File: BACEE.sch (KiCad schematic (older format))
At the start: 13 parts, among them U1 DS1337S+, U2 24LC1025, U3 24LC1025, U4 ATMEGA328P-AU, Y1 Crystal 32MHz, Y2 Crystal 16MHz

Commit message: Corrected the Atmega unconnected pins
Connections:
- no-connect marks 13 -> 7
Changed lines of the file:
@@
 	7800 4950 7800 5150
 $Comp
-L power:GNDPWR #PWR?
+L power:GNDPWR #PWR0101
 U 1 1 5EC52C1A
 P 4950 7400
-F 0 "#PWR?" H 4950 7200 50  0001 C CNN
+F 0 "#PWR0101" H 4950 7200 50  0001 C CNN
 F 1 "GNDPWR" H 4954 7246 50  0000 C CNN
 F 2 "" H 4950 7350 50  0001 C CNN
@@
 	650  1600 650  1650
 $Comp
-L power:GNDPWR #PWR?
+L power:GNDPWR #PWR0102
 U 1 1 5EC62315
 P 2100 2750
-F 0 "#PWR?" H 2100 2550 50  0001 C CNN
+F 0 "#PWR0102" H 2100 2550 50  0001 C CNN
 F 1 "GNDPWR" H 2104 2596 50  0000 C CNN
 F 2 "" H 2100 2700 50  0001 C CNN
@@
 Wire Wire Line
 	2750 2100 2900 2100
-NoConn ~ 2800 1700
 Text Label 2800 3900 2    50   ~ 0
 Vcc
@@
 	2750 3900 2800 3900
 $Comp
-L power:GNDPWR #PWR?
+L power:GNDPWR #PWR0103
 U 1 1 5EC69D54
 P 2750 5300
-F 0 "#PWR?" H 2750 5100 50  0001 C CNN
+F 0 "#PWR0103" H 2750 5100 50  0001 C CNN
 F 1 "GNDPWR" H 2754 5146 50  0000 C CNN
 F 2 "" H 2750 5250 50  0001 C CNN
@@
 Wire Wire Line
 	2750 4200 3350 4200
-Wire Wire Line
-	2000 4200 2750 4200
 Text Label 2400 4500 0    50   ~ 0
 SDA
@@
 ADDS2
 $Comp
-L power:GNDPWR #PWR?
+L power:GNDPWR #PWR0104
 U 1 1 5EC78DFA
 P 9750 3500
-F 0 "#PWR?" H 9750 3300 50  0001 C CNN
+F 0 "#PWR0104" H 9750 3300 50  0001 C CNN
 F 1 "GNDPWR" H 9754 3346 50  0000 C CNN
 F 2 "" H 9750 3450 50  0001 C CNN
@@
 	9750 2050 9750 1400
 Wire Wire Line
-	9750 1400 7900 1400
+	9750 1400 8700 1400
 Connection ~ 9750 2050
 Wire Wire Line
@@
 	6800 2450 7300 2450
 $Comp
-L power:GNDPWR #PWR?
+L power:GNDPWR #PWR0105
 U 1 1 5EC8EEE6
 P 4150 3100
-F 0 "#PWR?" H 4150 2900 50  0001 C CNN
+F 0 "#PWR0105" H 4150 2900 50  0001 C CNN
 F 1 "GNDPWR" H 4154 2946 50  0000 C CNN
 F 2 "" H 4150 3050 50  0001 C CNN
@@
 	5200 2800 5900 2800
 $Comp
-L power:GNDPWR #PWR?
+L power:GNDPWR #PWR0106
 U 1 1 5ECAE791
 P 5500 4100
-F 0 "#PWR?" H 5500 3900 50  0001 C CNN
+F 0 "#PWR0106" H 5500 3900 50  0001 C CNN
 F 1 "GNDPWR" H 5504 3946 50  0000 C CNN
 F 2 "" H 5500 4050 50  0001 C CNN
@@
 	6600 4700 6300 4700
 $Comp
-L power:GNDPWR #PWR?
+L power:GNDPWR #PWR0107
 U 1 1 5ECC3376
 P 7900 5500
-F 0 "#PWR?" H 7900 5300 50  0001 C CNN
+F 0 "#PWR0107" H 7900 5300 50  0001 C CNN
 F 1 "GNDPWR" H 7904 5346 50  0000 C CNN
 F 2 "" H 7900 5450 50  0001 C CNN
@@
 Wire Wire Line
 	7900 5150 7900 5500
-NoConn ~ 7300 2150
-NoConn ~ 7300 2250
-NoConn ~ 7300 2550
-NoConn ~ 7300 2650
-NoConn ~ 7300 2750
-NoConn ~ 7300 2850
-NoConn ~ 7300 3150
-NoConn ~ 7300 3250
 NoConn ~ 7300 3650
 NoConn ~ 7300 3750
 NoConn ~ 7300 4450
 NoConn ~ 7300 4650
+$Comp
+L power:PWR_FLAG #FLG0101
+U 1 1 5ECE3B27
+P 8700 1400
+F 0 "#FLG0101" H 8700 1475 50  0001 C CNN
+F 1 "PWR_FLAG" H 8700 1573 50  0000 C CNN
+F 2 "" H 8700 1400 50  0001 C CNN
+F 3 "~" H 8700 1400 50  0001 C CNN
+	1    8700 1400
+	1    0    0    -1
+$EndComp
+Connection ~ 8700 1400
+Wire Wire Line
+	8700 1400 7900 1400
+Wire Wire Line
+	2000 4200 2750 4200
+NoConn ~ 7300 2950
+NoConn ~ 7300 3050
+NoConn ~ 2750 1700
 $EndSCHEMATC

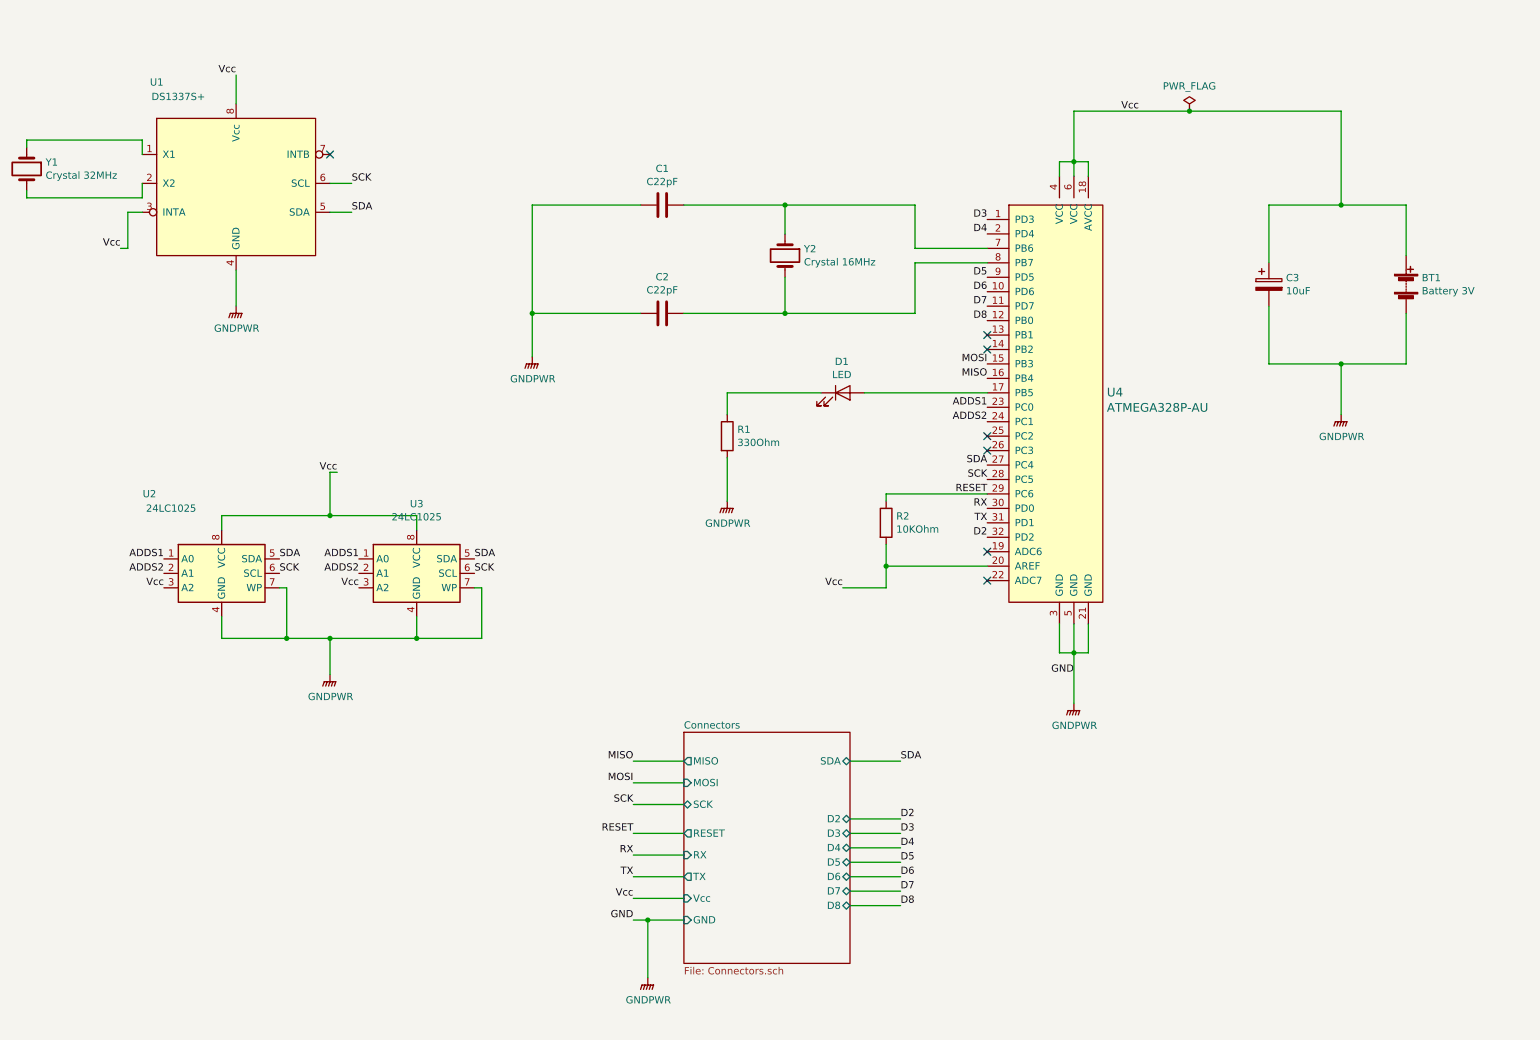
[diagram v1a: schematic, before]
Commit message: Added functional block descriptions
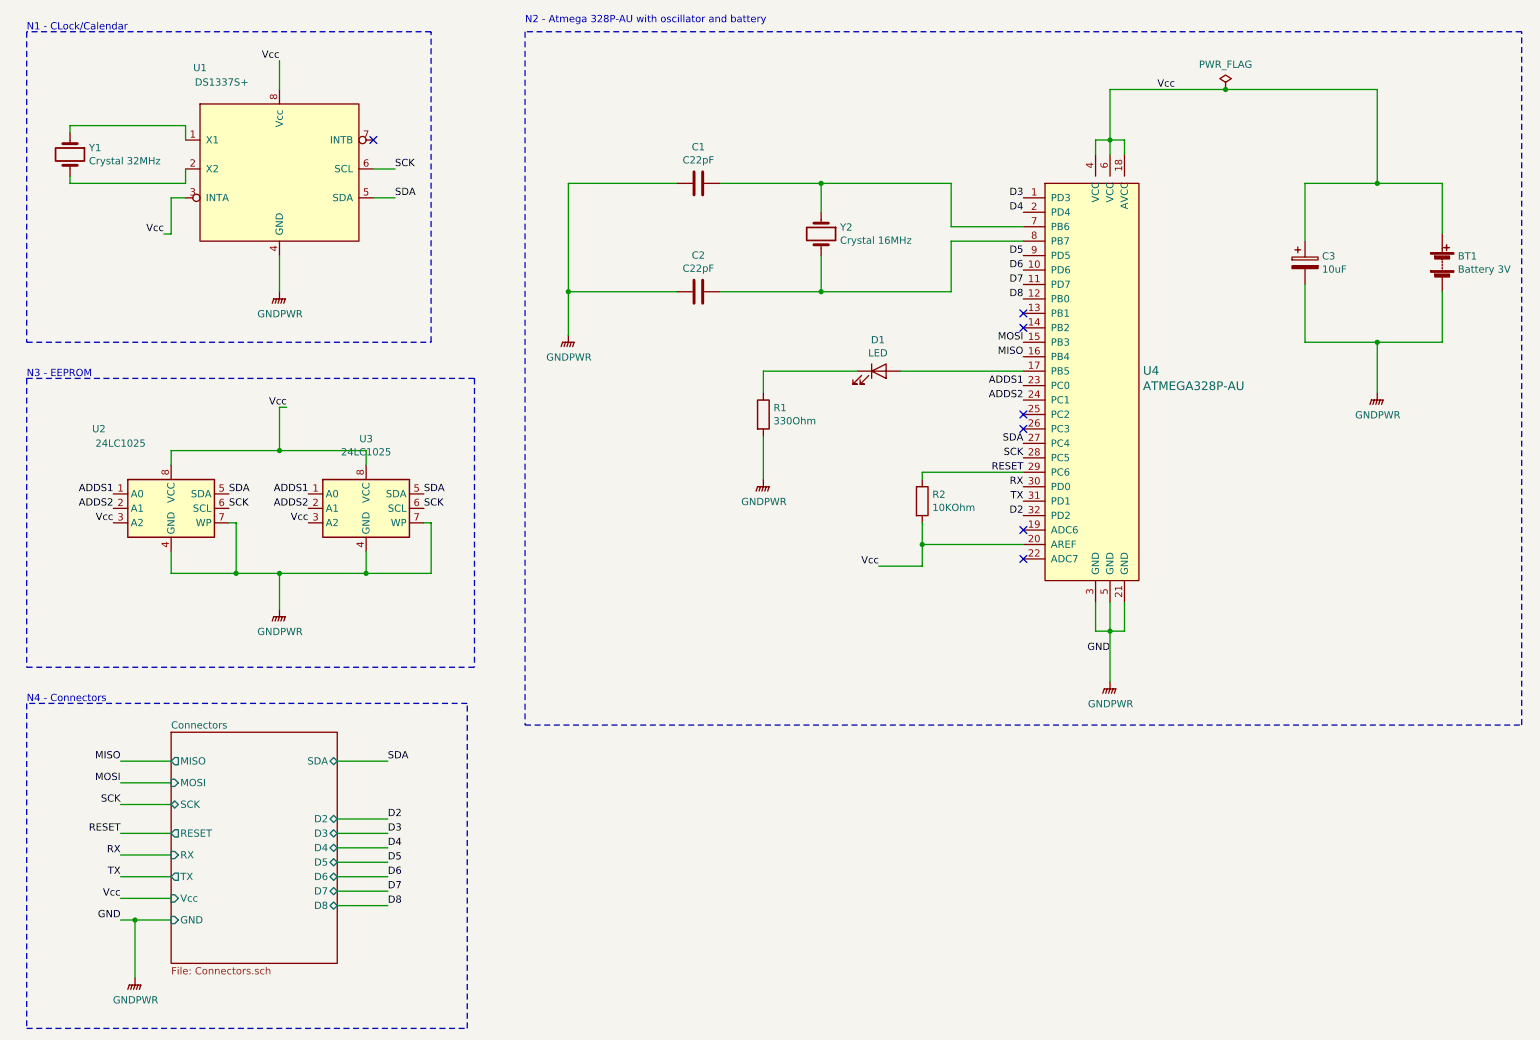
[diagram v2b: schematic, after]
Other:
- note added: "N1 - CLock/Calendar"
- note added: "N2 - Atmega 328P-AU with oscillator and battery"
- note added: "N3 - EEPROM"
- note added: "N4 - Connectors"
- moved on the sheet: BT1, C1, C2, C3, D1, R1, R2, U1, U2, U3, U4, Y1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
